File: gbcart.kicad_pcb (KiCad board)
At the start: 2 copper layers, 51.4 x 61 mm, 39 parts, among them J1 Conn_01x32, J2 USB_B_Micro, J3 Micro_SD_Card, J4 Conn_01x06_Male, J5 Conn_01x06_Male, Q1 BC847, SW1 SW_Push, U1 ESP32-S3-MINI-1, U2 74HC138, U3 74HCT1G125, U4 74HC259, U5 29F040-TSOP-SP, U6 74lxc125, U8 LD3985M33R_SOT23, U9 NC7SZ08

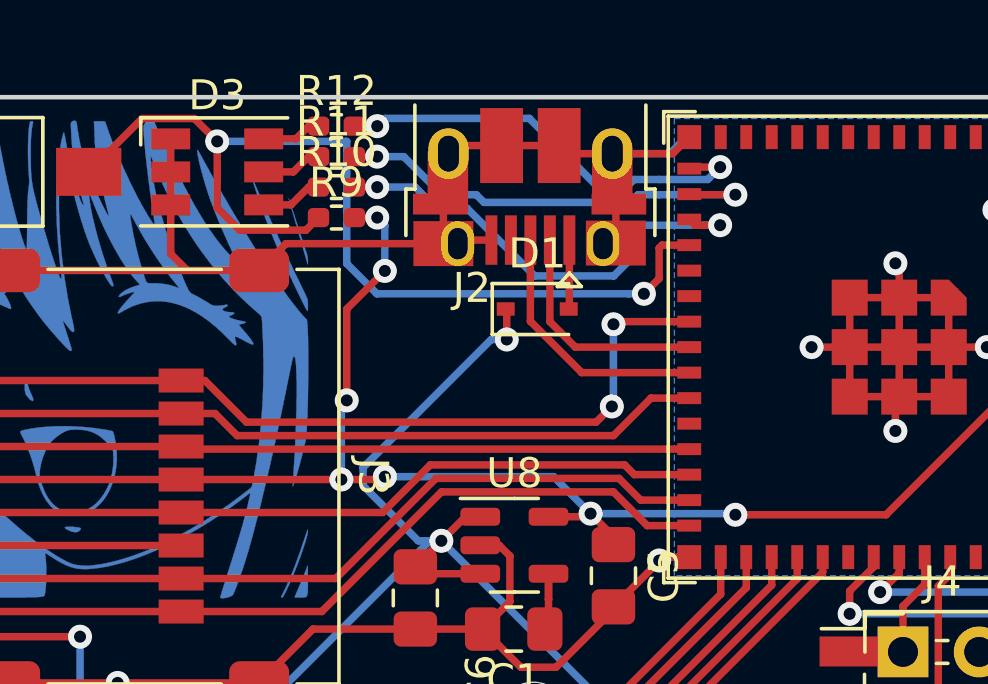
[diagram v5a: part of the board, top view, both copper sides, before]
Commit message: Move connections to avalible on esp32-s3-DevkitC
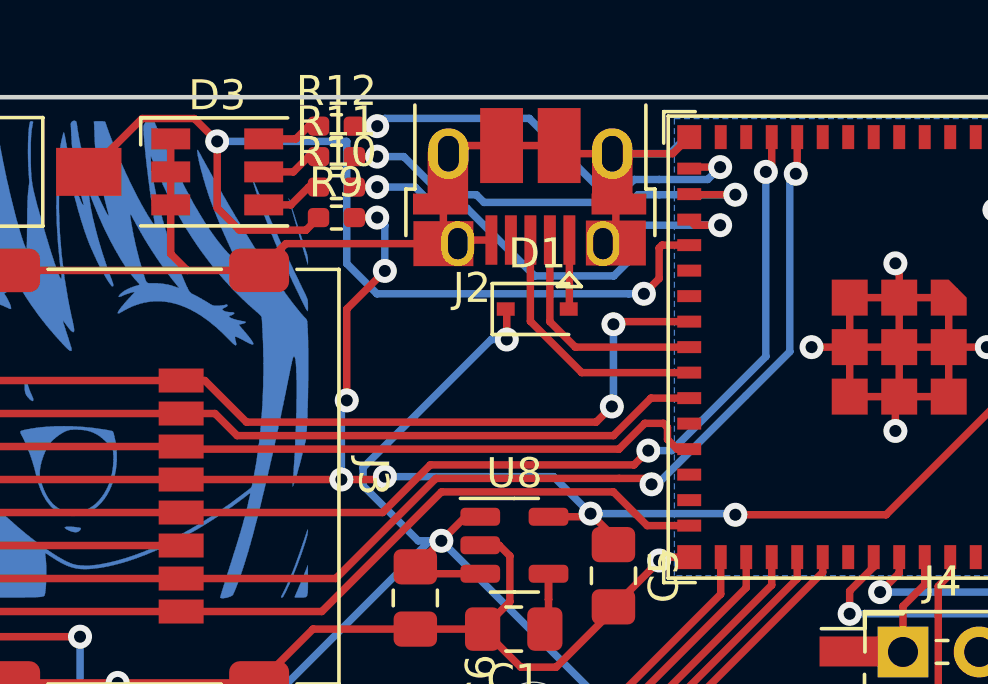
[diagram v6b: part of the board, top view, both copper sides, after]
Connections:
- U1 pad 12: unconnected-(U1-Pad12) -> /SD_DATA0
- U1 pad 13: unconnected-(U1-Pad13) -> /SD_CLOCK
- U1 pad 28: /SD_CLOCK -> unconnected-(U1-Pad28)
- U1 pad 29: /SD_DATA0 -> unconnected-(U1-Pad29)
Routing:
- net /SD_DATA0: track 29.7 -> 41.9 mm, vias 0 -> 2
- net /SD_CLOCK: track 28.7 -> 40.1 mm, vias 0 -> 2
- net /SD_CMD: track 28.1 -> 29.0 mm

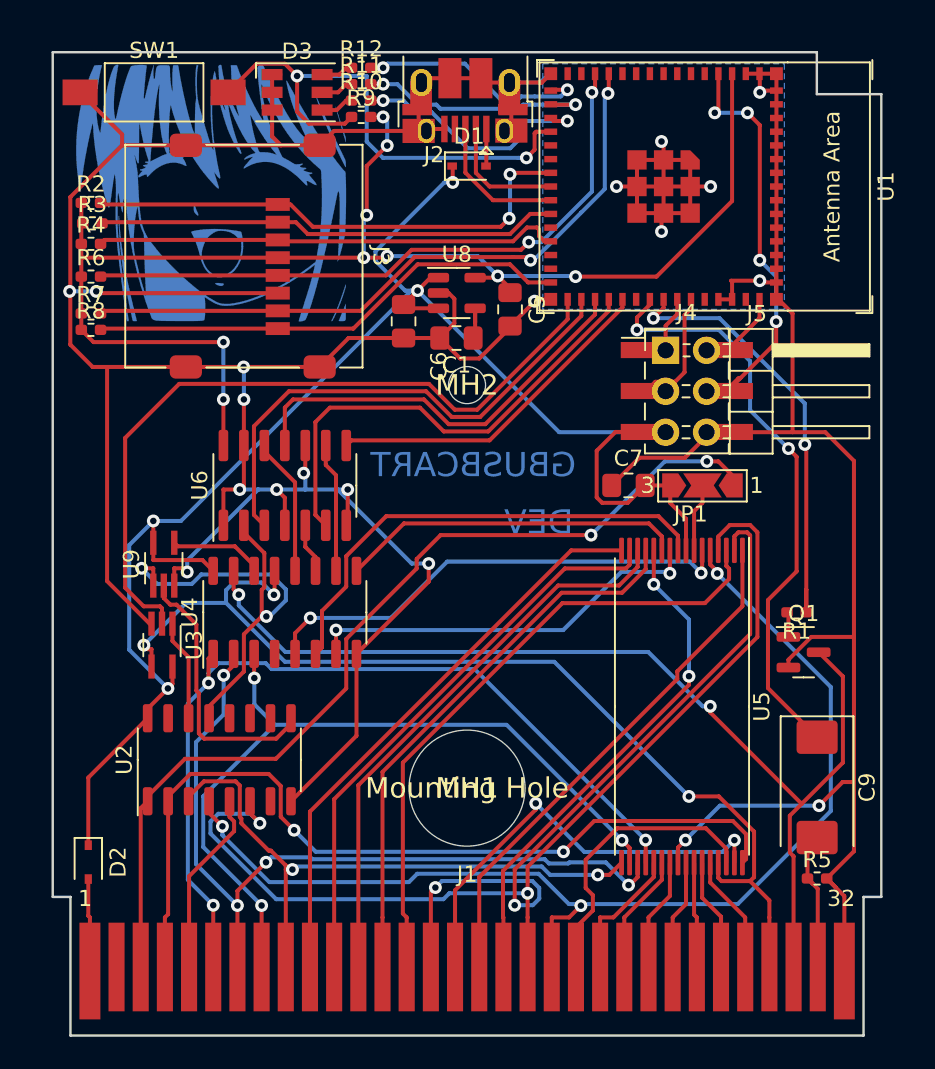
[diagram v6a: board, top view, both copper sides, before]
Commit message: Move reset to seperate IO pin
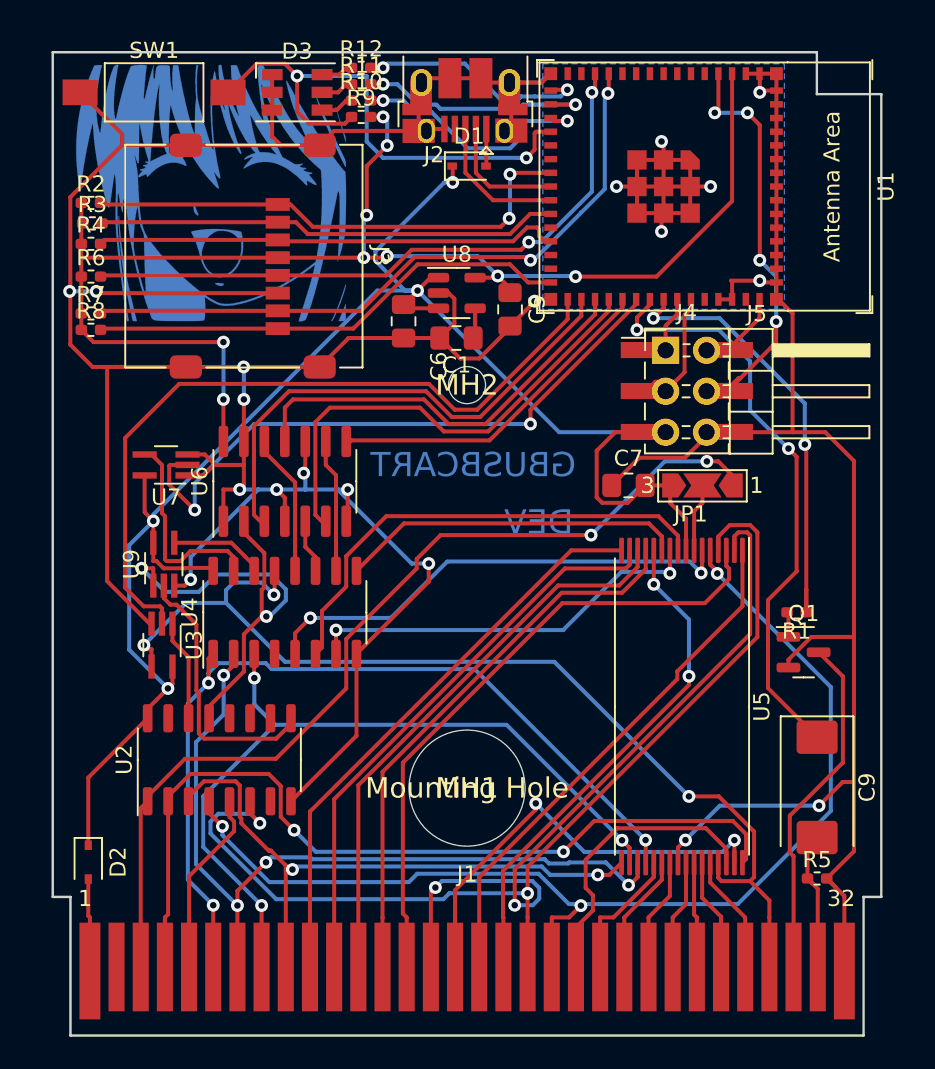
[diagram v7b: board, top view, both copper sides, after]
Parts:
- added U7: 74HCT1G125, Package_TO_SOT_SMD:SOT-353_SC-70-5_Handsoldering, F.Cu at (105.2, 85.6)
- moved U6 0.25 mm to (112.5, 86.6)
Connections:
- U1 pad 36: unconnected-(U1-Pad36) -> Net-(U7-Pad2)
- U4 pad 15: /GB.~{RST} -> Net-(U4-Pad15)
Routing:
- net /GB.~{RST}: track 66.7 -> 24.1 mm, vias 2 -> 0
- net Net-(U7-Pad2): track 0.00 -> 39.0 mm, vias 0 -> 2
- net Net-(U4-Pad15): track 0.00 -> 12.2 mm
- net GND: track 318.2 -> 323.5 mm
- net +5V: track 106.5 -> 109.9 mm

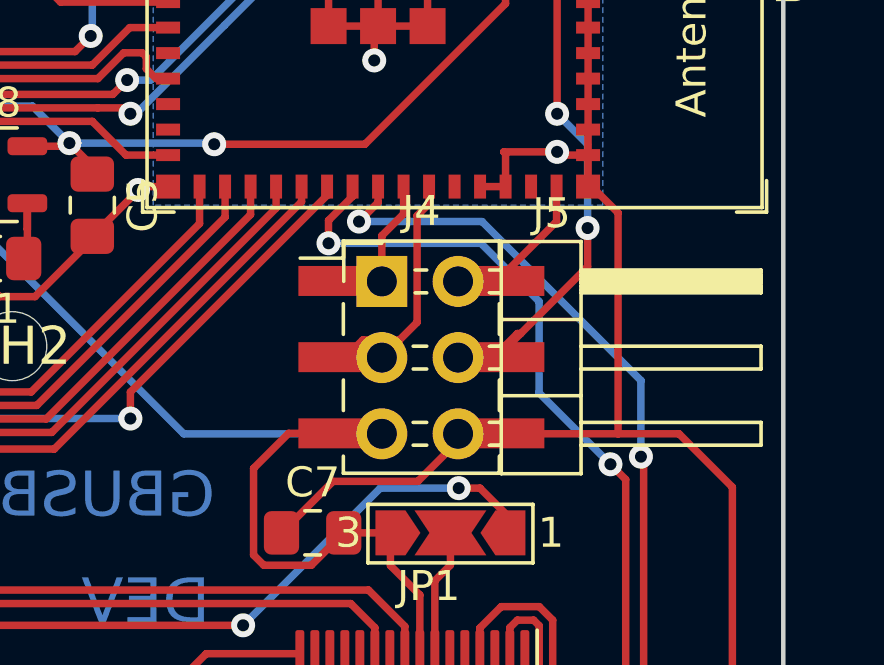
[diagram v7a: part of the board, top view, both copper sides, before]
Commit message: Move connector + add silkscren names
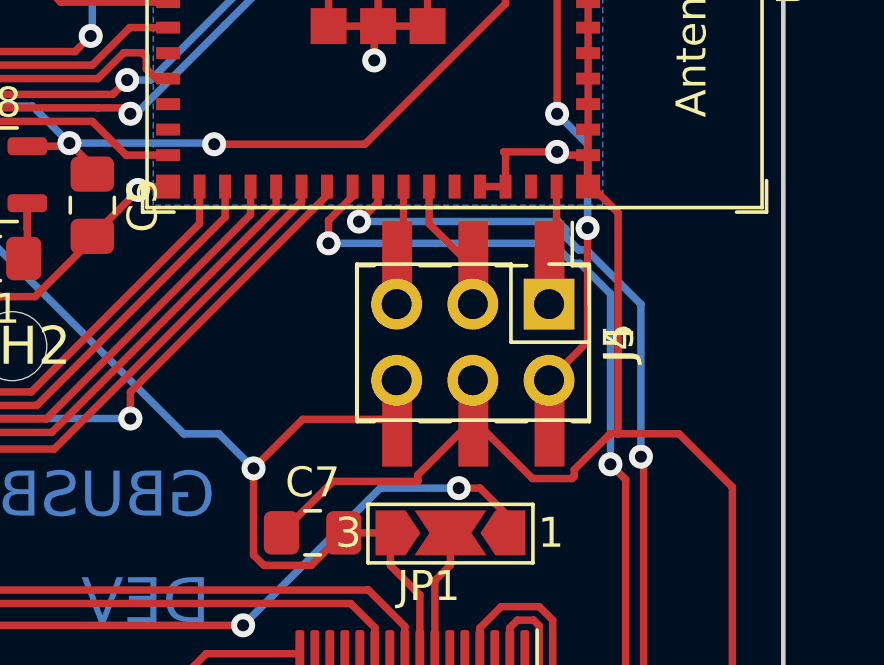
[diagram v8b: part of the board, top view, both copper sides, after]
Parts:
- J5: footprint Connector_PinHeader_2.54mm:PinHeader_2x03_P2.54mm_Horizontal -> Connector_PinHeader_2.54mm:PinHeader_2x03_P2.54mm_Vertical
- moved J5 5.62 mm to (141.7, 79.2), turned to -90 degrees
- moved J4 1.79 mm to (139.2, 80.6), turned to -90 degrees
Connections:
- J4 pad 1: /DTX_E -> /DRTS
- J4 pad 2: /DRTS -> /DDTR
- J4 pad 4: /DDTR -> GND
- J4 pad 5: +5V -> /DTX_E
- J4 pad 6: GND -> +5V
- J5 pad 1: /DTX_E -> /DRTS
- J5 pad 2: /DRTS -> /DDTR
- J5 pad 4: /DDTR -> GND
- J5 pad 5: +5V -> /DTX_E
- J5 pad 6: GND -> +5V
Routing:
- net /DRX_E: track 8.38 -> 3.32 mm
- net +5V: track 109.9 -> 106.8 mm, vias 4 -> 5
- net /DRTS: track 5.27 -> 2.81 mm
- net /DDTR: track 26.2 -> 23.9 mm
- net /DTX_E: track 4.82 -> 2.80 mm
- net Net-(R1-Pad1): track 27.4 -> 29.1 mm
- net GND: track 323.5 -> 325.1 mm
- net Net-(C9-Pad1): track 36.6 -> 38.1 mm
